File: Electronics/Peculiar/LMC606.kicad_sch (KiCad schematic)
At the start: 12 parts, among them U14 ${SIM.PARAMS}, U15 ${SIM.PARAMS}

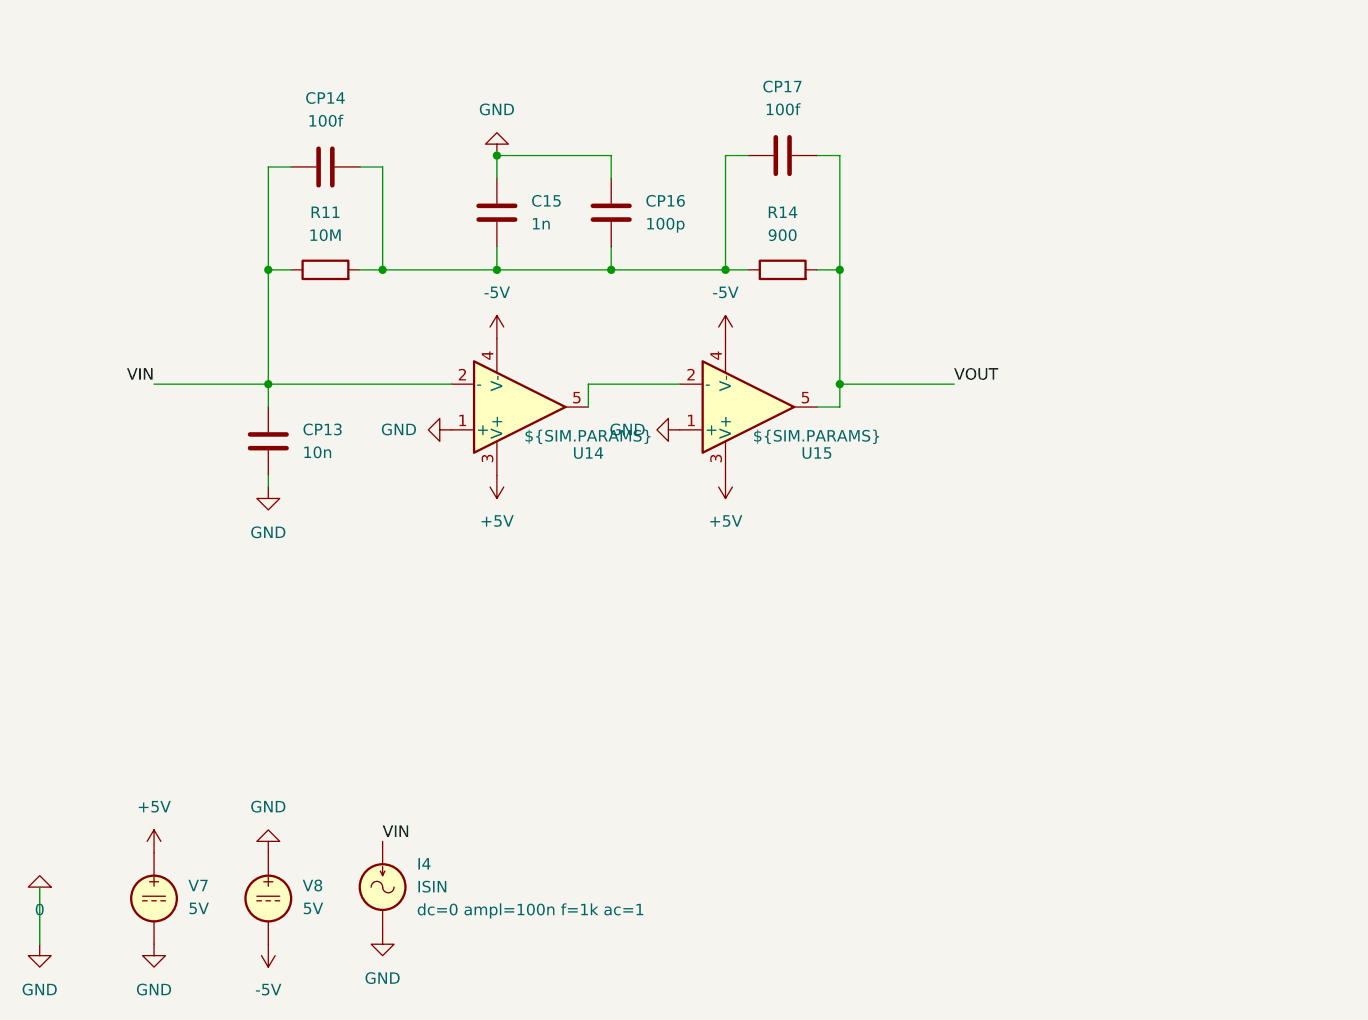
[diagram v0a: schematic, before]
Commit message: Add LMC606 to simulation
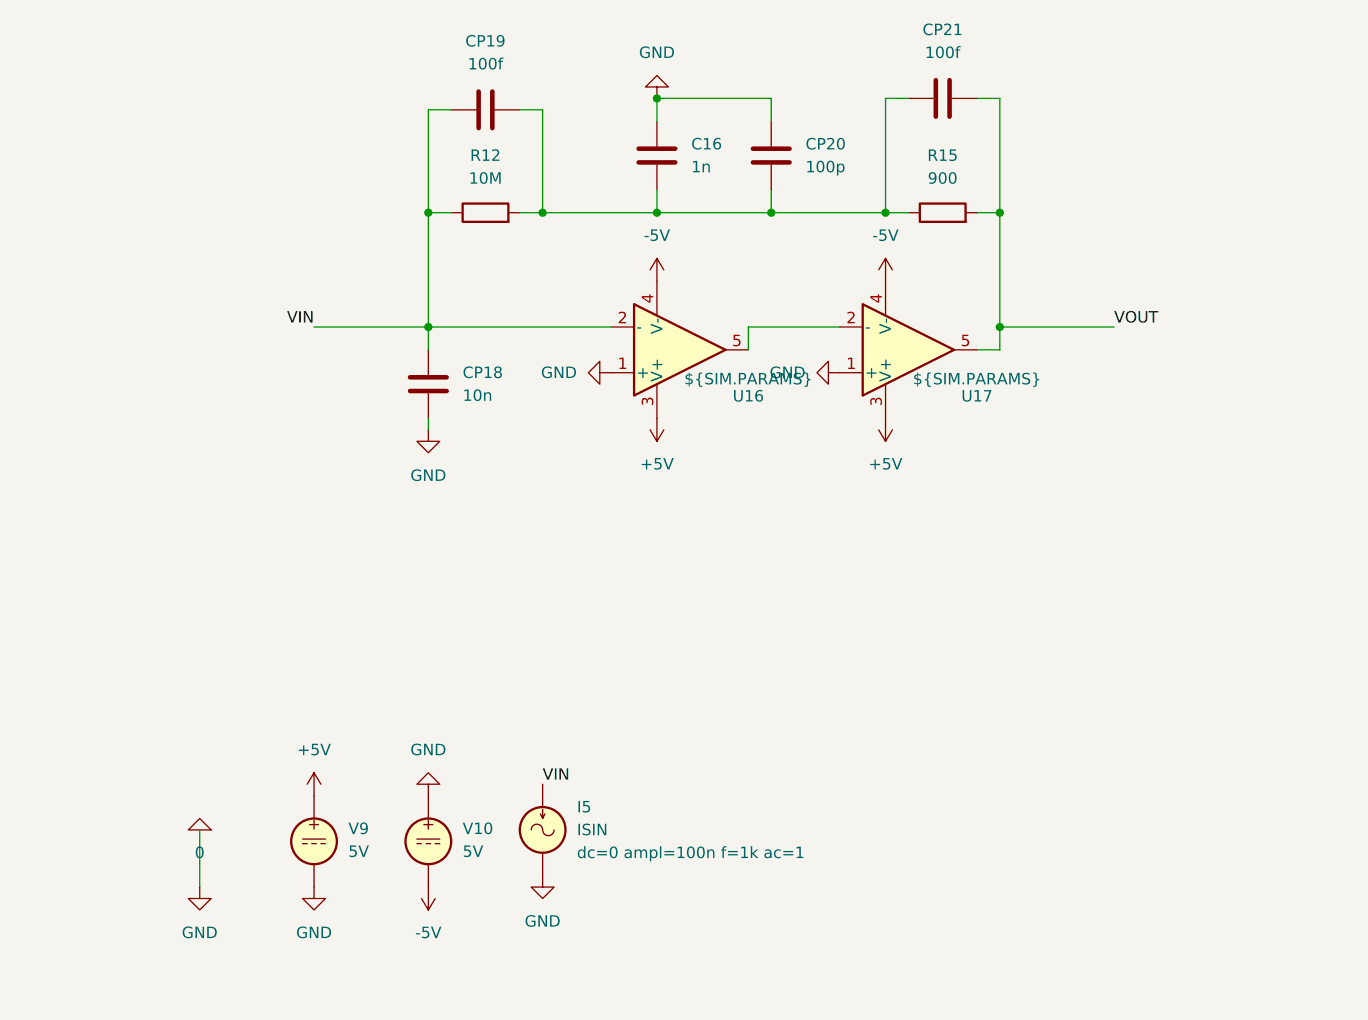
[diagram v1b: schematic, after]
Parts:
- removed C15: 1n, symbol Device:C
- removed CP13: 10n, symbol Device:C
- removed CP14, CP17: 100f, symbol Device:C
- removed CP16: 100p, symbol Device:C
- removed I4: ISIN, symbol Simulation_SPICE:ISIN
- removed R11: 10M, symbol Device:R
- removed R14: 900, symbol Device:R
- removed U14, U15: ${SIM.PARAMS}, symbol Simulation_SPICE:OPAMP
- removed V7, V8: 5V, symbol Simulation_SPICE:VDC
- added C16: 1n, symbol Device:C
- added CP18: 10n, symbol Device:C
- added CP19, CP21: 100f, symbol Device:C
- added CP20: 100p, symbol Device:C
- added I5: ISIN, symbol Simulation_SPICE:ISIN
- added R12: 10M, symbol Device:R
- added R15: 900, symbol Device:R
- added U16, U17: ${SIM.PARAMS}, symbol Simulation_SPICE:OPAMP
- added V10, V9: 5V, symbol Simulation_SPICE:VDC
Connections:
- net +5V: now also U16.3 (V+), U17.3 (V+), V9.1
- net -5V: now also U16.4 (V-), U17.4 (V-), V10.2
- net 0: now also C16.2, CP18.2, CP20.2, I5.2, U16.1 (+), U17.1 (+), V10.1, V9.2
- net VIN: now also CP18.1, CP19.1, I5.1, R12.1, U16.2 (-)
- net VOUT: now also CP21.2, R15.2, U17.5
- new net: C16.1, CP19.2, CP20.1, CP21.1, R12.2, R15.1
- new net: U16.5, U17.2 (-)

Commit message: Create some other simulations
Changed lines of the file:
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@@
-	)
-	(junction
-		(at 182.88 95.25)
-		(diameter 0)
-		(color 0 0 0 0)
 	)
 	(junction
@@
 	)
 	(junction
+		(at 203.2 82.55)
+		(diameter 0)
+		(color 0 0 0 0)
+	)
+	(junction
 		(at 119.38 82.55)
 		(diameter 0)
@@
 	)
 	(junction
-		(at 182.88 82.55)
+		(at 203.2 95.25)
 		(diameter 0)
 		(color 0 0 0 0)
@@
 	(wire
 		(pts
-			(xy 182.88 95.25) (xy 195.58 95.25)
+			(xy 203.2 95.25) (xy 215.9 95.25)
 		)
 		(stroke
@@
 	(wire
 		(pts
-			(xy 182.88 82.55) (xy 182.88 95.25)
-		)
-		(stroke
-			(width 0)
-			(type default)
-		)
-	)
-	(wire
-		(pts
-			(xy 182.88 69.85) (xy 182.88 82.55)
+			(xy 203.2 82.55) (xy 203.2 95.25)
+		)
+		(stroke
+			(width 0)
+			(type default)
+		)
+	)
+	(wire
+		(pts
+			(xy 180.34 95.25) (xy 203.2 95.25)
+		)
+		(stroke
+			(width 0)
+			(type default)
+		)
+	)
+	(wire
+		(pts
+			(xy 203.2 69.85) (xy 203.2 82.55)
 		)
 		(stroke
@@
 	(wire
 		(pts
-			(xy 180.34 97.79) (xy 182.88 97.79)
-		)
-		(stroke
-			(width 0)
-			(type default)
-		)
-	)
-	(wire
-		(pts
-			(xy 180.34 82.55) (xy 182.88 82.55)
+			(xy 180.34 82.55) (xy 203.2 82.55)
 		)
 		(stroke
@@
 	(wire
 		(pts
+			(xy 180.34 97.79) (xy 180.34 95.25)
+		)
+		(stroke
+			(width 0)
+			(type default)
+		)
+	)
+	(wire
+		(pts
 			(xy 157.48 82.55) (xy 170.18 82.55)
 		)
@@
 	(wire
 		(pts
-			(xy 182.88 95.25) (xy 182.88 97.79)
-		)
-		(stroke
-			(width 0)
-			(type default)
-		)
-	)
-	(wire
-		(pts
 			(xy 119.38 97.79) (xy 119.38 95.25)
 		)
@@
 	(wire
 		(pts
-			(xy 180.34 69.85) (xy 182.88 69.85)
+			(xy 180.34 69.85) (xy 203.2 69.85)
 		)
 		(stroke
@@
 	)
 	(label "VOUT"
-		(at 195.58 95.25 0)
+		(at 215.9 95.25 0)
 		(effects
 			(font

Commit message: Create a great design using OPA858 and OPA162
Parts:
- renumbered C16 to C8, CP19 to CP10, CP20 to CP11, CP21 to CP12, CP18 to CP9, R12 to R11, R15 to R12, U16 to U10, U17 to U11
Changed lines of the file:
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@@
 		(dnp no)
 		(fields_autoplaced yes)
-		(property "Reference" "R15"
+		(property "Reference" "R12"
 			(at 176.53 76.2 90)
 			(show_name no)
@@
 			(project "Peculiar"
 				(path "/db27cf5d-1015-467f-a739-ab2eb7f0a1b5/7635d485-3c10-4c21-b915-82aca00c633b"
-					(reference "R15")
+					(reference "R12")
 					(unit 1)
 				)
@@
 		(dnp no)
 		(fields_autoplaced yes)
-		(property "Reference" "CP19"
+		(property "Reference" "CP10"
 			(at 125.73 63.5 90)
 			(show_name no)
@@
 			(project "Peculiar"
 				(path "/db27cf5d-1015-467f-a739-ab2eb7f0a1b5/7635d485-3c10-4c21-b915-82aca00c633b"
-					(reference "CP19")
+					(reference "CP10")
 					(unit 1)
 				)
@@
 		(dnp no)
 		(fields_autoplaced yes)
-		(property "Reference" "CP18"
+		(property "Reference" "CP9"
 			(at 123.19 100.3299 0)
 			(show_name no)
@@
 			(project "Peculiar"
 				(path "/db27cf5d-1015-467f-a739-ab2eb7f0a1b5/7635d485-3c10-4c21-b915-82aca00c633b"
-					(reference "CP18")
+					(reference "CP9")
 					(unit 1)
 				)
@@
 		(in_pos_files yes)
 		(dnp no)
-		(property "Reference" "U16"
+		(property "Reference" "U10"
 			(at 154.94 102.9402 0)
 			(show_name no)
@@
 			(project "Peculiar"
 				(path "/db27cf5d-1015-467f-a739-ab2eb7f0a1b5/7635d485-3c10-4c21-b915-82aca00c633b"
-					(reference "U16")
+					(reference "U10")
 					(unit 1)
 				)
@@
 		(dnp no)
 		(fields_autoplaced yes)
-		(property "Reference" "R12"
+		(property "Reference" "R11"
 			(at 125.73 76.2 90)
 			(show_name no)
@@
 			(project "Peculiar"
 				(path "/db27cf5d-1015-467f-a739-ab2eb7f0a1b5/7635d485-3c10-4c21-b915-82aca00c633b"
-					(reference "R12")
+					(reference "R11")
 					(unit 1)
 				)
@@
 		(dnp no)
 		(fields_autoplaced yes)
-		(property "Reference" "C16"
+		(property "Reference" "C8"
 			(at 148.59 74.9299 0)
 			(show_name no)
@@
 			(project "Peculiar"
 				(path "/db27cf5d-1015-467f-a739-ab2eb7f0a1b5/7635d485-3c10-4c21-b915-82aca00c633b"
-					(reference "C16")
+					(reference "C8")
 					(unit 1)
 				)
@@
 		(in_pos_files yes)
 		(dnp no)
-		(property "Reference" "U17"
+		(property "Reference" "U11"
 			(at 180.34 102.9402 0)
 			(show_name no)
@@
 			(project "Peculiar"
 				(path "/db27cf5d-1015-467f-a739-ab2eb7f0a1b5/7635d485-3c10-4c21-b915-82aca00c633b"
-					(reference "U17")
+					(reference "U11")
 					(unit 1)
 				)
@@
 		(dnp no)
 		(fields_autoplaced yes)
-		(property "Reference" "CP21"
+		(property "Reference" "CP12"
 			(at 176.53 62.23 90)
 			(show_name no)
@@
 			(project "Peculiar"
 				(path "/db27cf5d-1015-467f-a739-ab2eb7f0a1b5/7635d485-3c10-4c21-b915-82aca00c633b"
-					(reference "CP21")
+					(reference "CP12")
 					(unit 1)
 				)
@@
 		(dnp no)
 		(fields_autoplaced yes)
-		(property "Reference" "CP20"
+		(property "Reference" "CP11"
 			(at 161.29 74.9299 0)
 			(show_name no)
@@
 			(project "Peculiar"
 				(path "/db27cf5d-1015-467f-a739-ab2eb7f0a1b5/7635d485-3c10-4c21-b915-82aca00c633b"
-					(reference "CP20")
-					(unit 1)
-				)
+					(reference "CP11")
+					(unit 1)
+				)
